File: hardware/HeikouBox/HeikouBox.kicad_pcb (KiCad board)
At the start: 2 copper layers, 0 parts

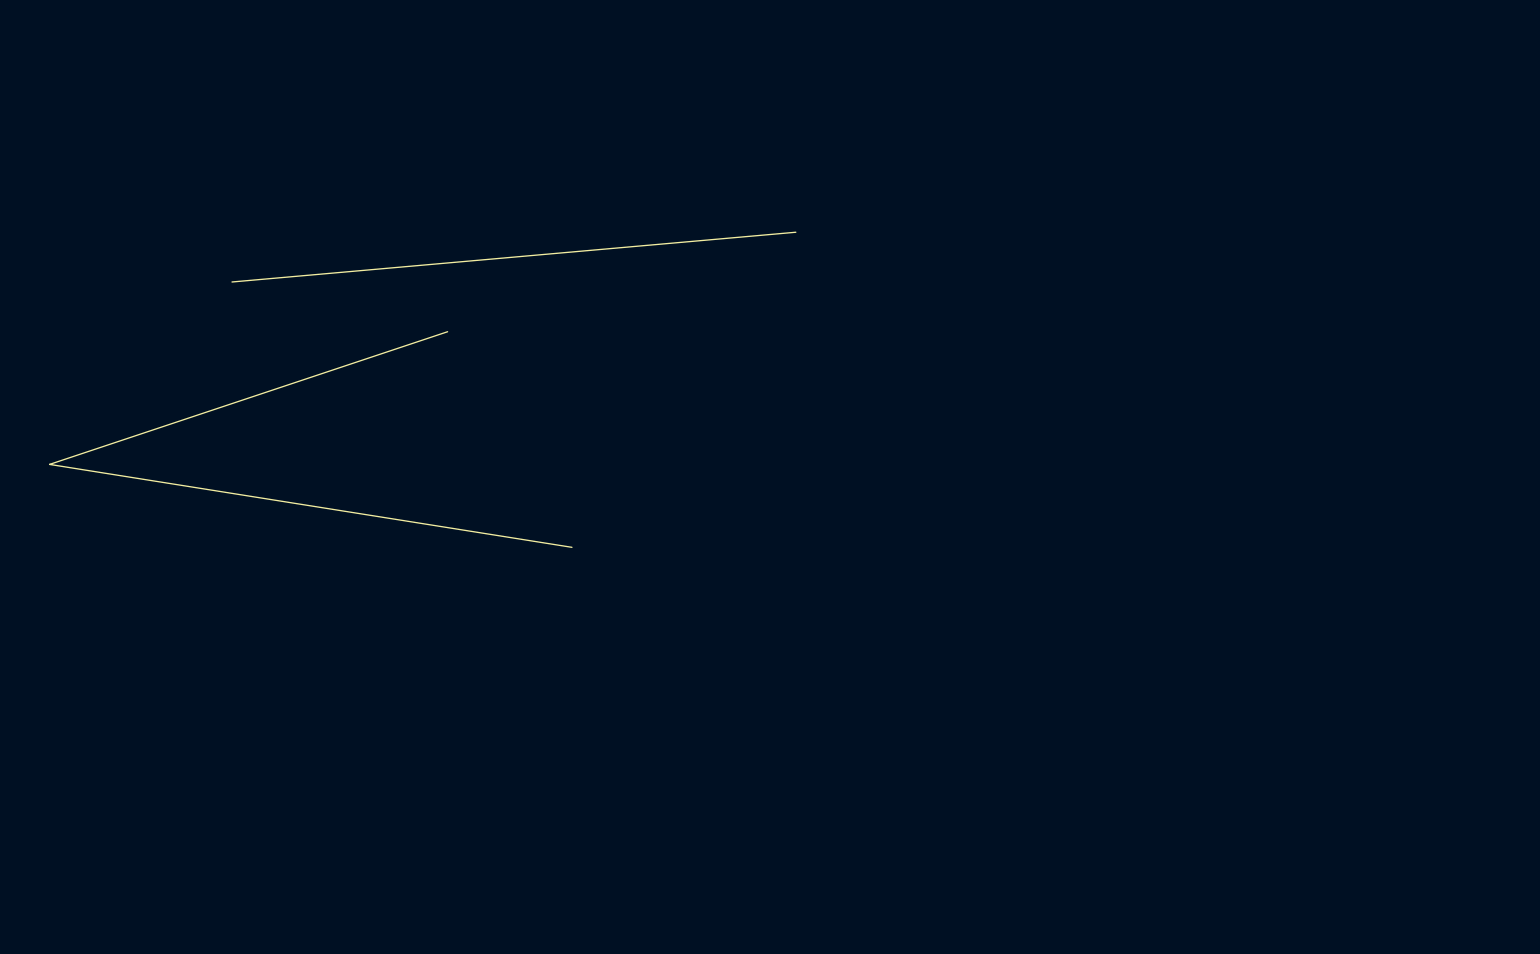
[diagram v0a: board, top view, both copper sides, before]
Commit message: Tidy up and split to multi sheet
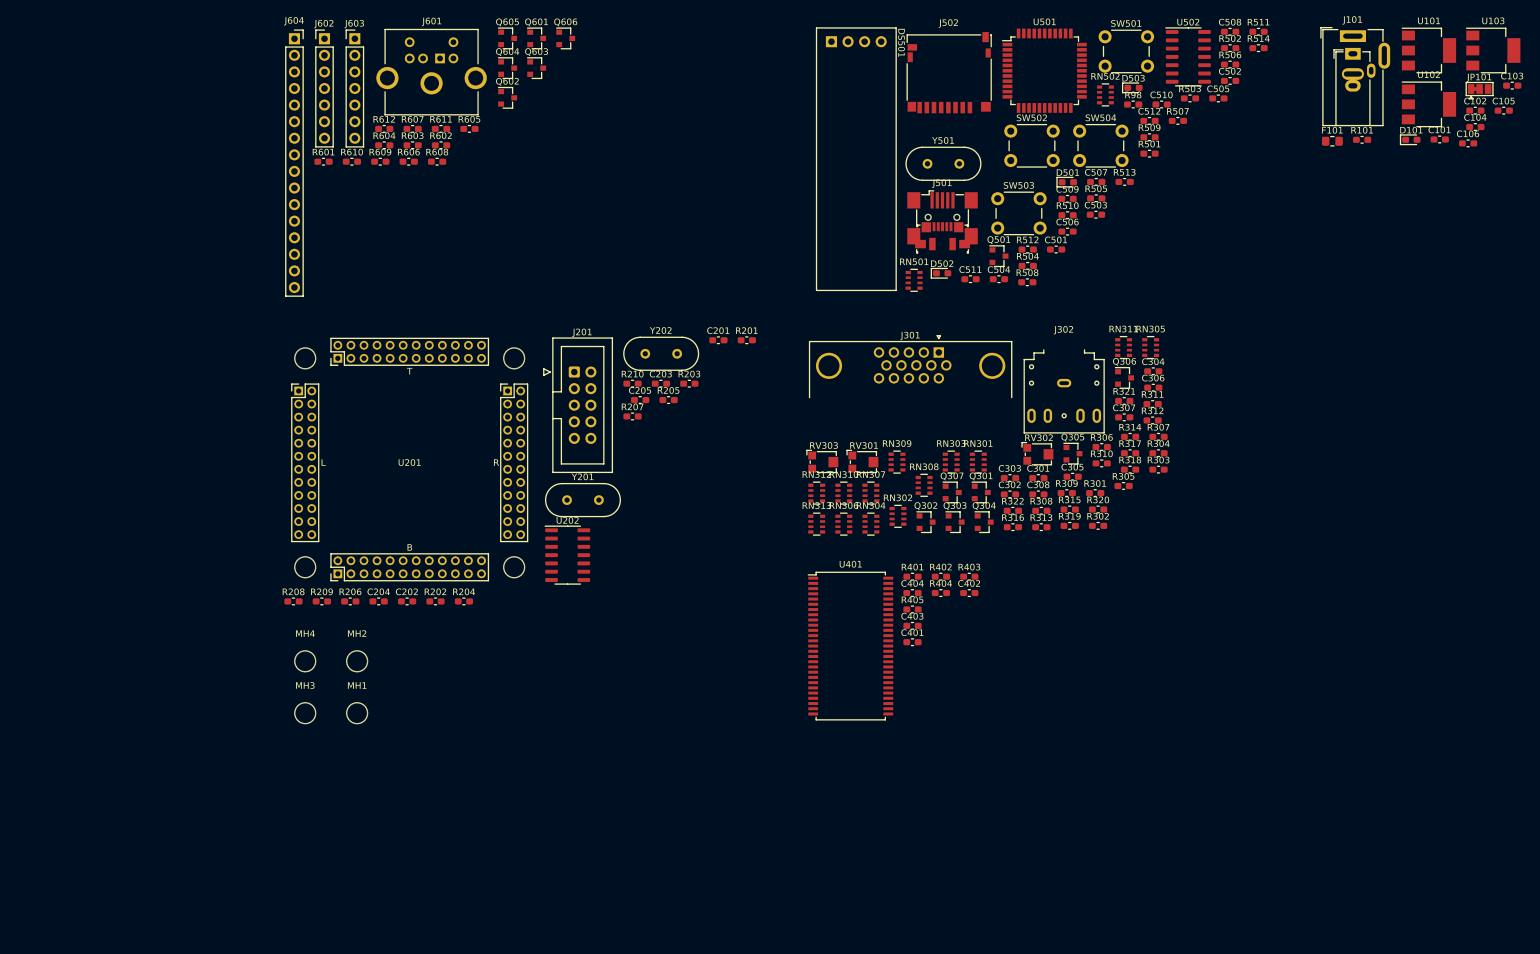
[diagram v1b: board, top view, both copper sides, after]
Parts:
- added C101: 10u, Capacitor_SMD:C_0603_1608Metric_Pad1.05x0.95mm_HandSolder, F.Cu at (233.2, 34.1)
- added C102: 100n, Capacitor_SMD:C_0603_1608Metric_Pad1.05x0.95mm_HandSolder, F.Cu at (238.7, 29.6)
- added C103: 100n, Capacitor_SMD:C_0603_1608Metric_Pad1.05x0.95mm_HandSolder, F.Cu at (244.3, 25.8)
- added C104: 10u, Capacitor_SMD:C_0603_1608Metric_Pad1.05x0.95mm_HandSolder, F.Cu at (238.7, 32.1)
- added C105: 10u, Capacitor_SMD:C_0603_1608Metric_Pad1.05x0.95mm_HandSolder, F.Cu at (243.0, 29.6)
- added C106: 10u, Capacitor_SMD:C_0603_1608Metric_Pad1.05x0.95mm_HandSolder, F.Cu at (237.6, 34.7)
- added C201: 100n, Capacitor_SMD:C_0603_1608Metric_Pad1.05x0.95mm_HandSolder, F.Cu at (122.8, 64.8)
- added C202: 22p, Capacitor_SMD:C_0603_1608Metric_Pad1.05x0.95mm_HandSolder, F.Cu at (75.1, 104.8)
- added C203: 22p, Capacitor_SMD:C_0603_1608Metric_Pad1.05x0.95mm_HandSolder, F.Cu at (114.0, 71.5)
- added C204: 22p, Capacitor_SMD:C_0603_1608Metric_Pad1.05x0.95mm_HandSolder, F.Cu at (70.7, 104.8)
- added C205: 22p, Capacitor_SMD:C_0603_1608Metric_Pad1.05x0.95mm_HandSolder, F.Cu at (110.8, 74.0)
- added C301: 10u, Capacitor_SMD:C_0603_1608Metric_Pad1.05x0.95mm_HandSolder, F.Cu at (171.8, 85.9)
- added C302: 10u, Capacitor_SMD:C_0603_1608Metric_Pad1.05x0.95mm_HandSolder, F.Cu at (167.4, 88.4)
- added C303: 10n, Capacitor_SMD:C_0603_1608Metric_Pad1.05x0.95mm_HandSolder, F.Cu at (167.4, 85.9)
- added C304: 10n, Capacitor_SMD:C_0603_1608Metric_Pad1.05x0.95mm_HandSolder, F.Cu at (189.4, 69.6)
- added C305: 1u, Capacitor_SMD:C_0603_1608Metric_Pad1.05x0.95mm_HandSolder, F.Cu at (177.0, 85.7)
- added C306: 1u, Capacitor_SMD:C_0603_1608Metric_Pad1.05x0.95mm_HandSolder, F.Cu at (189.4, 72.1)
- added C307: 1u, Capacitor_SMD:C_0603_1608Metric_Pad1.05x0.95mm_HandSolder, F.Cu at (184.9, 76.6)
- added C308: 1u, Capacitor_SMD:C_0603_1608Metric_Pad1.05x0.95mm_HandSolder, F.Cu at (171.8, 88.4)
- added C401: 100n, Capacitor_SMD:C_0603_1608Metric_Pad1.05x0.95mm_HandSolder, F.Cu at (152.5, 111.1)
- added C402: 100n, Capacitor_SMD:C_0603_1608Metric_Pad1.05x0.95mm_HandSolder, F.Cu at (161.2, 103.5)
- added C403: 100n, Capacitor_SMD:C_0603_1608Metric_Pad1.05x0.95mm_HandSolder, F.Cu at (152.5, 108.5)
- added C404: 100n, Capacitor_SMD:C_0603_1608Metric_Pad1.05x0.95mm_HandSolder, F.Cu at (152.5, 103.5)
- added C501: 100n, Capacitor_SMD:C_0603_1608Metric_Pad1.05x0.95mm_HandSolder, F.Cu at (174.5, 50.9)
- added C502: 100n, Capacitor_SMD:C_0603_1608Metric_Pad1.05x0.95mm_HandSolder, F.Cu at (201.1, 25.1)
- added C503: 100n, Capacitor_SMD:C_0603_1608Metric_Pad1.05x0.95mm_HandSolder, F.Cu at (180.6, 45.6)
- added C504: 100n, Capacitor_SMD:C_0603_1608Metric_Pad1.05x0.95mm_HandSolder, F.Cu at (165.7, 55.5)
- added C505: 100n, Capacitor_SMD:C_0603_1608Metric_Pad1.05x0.95mm_HandSolder, F.Cu at (199.3, 27.8)
- added C506: 100n, Capacitor_SMD:C_0603_1608Metric_Pad1.05x0.95mm_HandSolder, F.Cu at (176.2, 48.2)
- added C507: 22p, Capacitor_SMD:C_0603_1608Metric_Pad1.05x0.95mm_HandSolder, F.Cu at (180.6, 40.6)
- added C508: 22p, Capacitor_SMD:C_0603_1608Metric_Pad1.05x0.95mm_HandSolder, F.Cu at (201.1, 17.6)
- added C509: 100n, Capacitor_SMD:C_0603_1608Metric_Pad1.05x0.95mm_HandSolder, F.Cu at (176.2, 43.1)
- added C510: 100n, Capacitor_SMD:C_0603_1608Metric_Pad1.05x0.95mm_HandSolder, F.Cu at (190.6, 28.7)
- added C511: 100n, Capacitor_SMD:C_0603_1608Metric_Pad1.05x0.95mm_HandSolder, F.Cu at (161.4, 55.5)
- added C512: 100n, Capacitor_SMD:C_0603_1608Metric_Pad1.05x0.95mm_HandSolder, F.Cu at (188.8, 31.2)
- added D101: Power, LED_SMD:LED_0603_1608Metric_Pad1.05x0.95mm_HandSolder, F.Cu at (228.9, 34.1)
- added D501: RX, LED_SMD:LED_0603_1608Metric_Pad1.05x0.95mm_HandSolder, F.Cu at (176.3, 40.6)
- added D502: TX, LED_SMD:LED_0603_1608Metric_Pad1.05x0.95mm_HandSolder, F.Cu at (157.0, 54.5)
- added D503: LOAD, LED_SMD:LED_0603_1608Metric_Pad1.05x0.95mm_HandSolder, F.Cu at (186.3, 26.1)
- added DS501: OLED-4P-I2C, KSK_HeikouBox:OLED-4P-Generic-128x32-0.91in, F.Cu at (140.1, 19.1)
- added F101: Poly 0.5A, Fuse:Fuse_0805_2012Metric_Pad1.15x1.40mm_HandSolder, F.Cu at (216.8, 34.3)
- added J101: Barrel_Jack_Switch, KSK_HeikouBox:BarrelJack_Multi, F.Cu at (219.9, 18.2)
- added J201: Conn_02x05_Odd_Even, Connector_IDC:IDC-Header_2x05_P2.54mm_Vertical, F.Cu at (100.7, 69.7)
- added J301: DB15_Female_HighDensity_MountingHoles, Connector_Dsub:DSUB-15-HD_Female_Horizontal_P2.29x1.98mm_EdgePinOffset3.03mm_Housed_MountingHolesOffset4.94mm, F.Cu at (156.5, 66.7)
- added J302: AudioJack3_SwitchTR, KSK_HeikouBox:Jack_3.5mm_PJ307_Horizontal_NoHoles, F.Cu at (175.7, 71.4)
- added J501: USB_B_Micro, KSK_HeikouBox:USB_Mini-Micro-B_Multi, F.Cu at (157.1, 46.0)
- added J502: Micro_SD_Card_Det, Connector_Card:microSD_HC_Hirose_DM3D-SF, F.Cu at (158.1, 23.8)
- added J601: PS/2 Keyboard, KSK_HeikouBox:TE_Mini-DIN-6_Horizontal, F.Cu at (80.1, 21.6)
- added J602: Conn_01x07, Connector_PinHeader_2.54mm:PinHeader_1x07_P2.54mm_Vertical, F.Cu at (62.4, 18.6)
- added J603: Conn_01x07, Connector_PinHeader_2.54mm:PinHeader_1x07_P2.54mm_Vertical, F.Cu at (67.1, 18.6)
- added J604: Conn_01x16, Connector_PinSocket_2.54mm:PinSocket_1x16_P2.54mm_Vertical, F.Cu at (57.8, 18.6)
- added JP101: SolderJumper_3_Bridged12, Jumper:SolderJumper-3_P1.3mm_Bridged12_Pad1.0x1.5mm, F.Cu at (239.3, 26.3)
- added MH1: MountingHole, MountingHole:MountingHole_3.2mm_M3, F.Cu at (67.4, 121.9)
- added MH2: MountingHole, MountingHole:MountingHole_3.2mm_M3, F.Cu at (67.4, 114.0)
- added MH3: MountingHole, MountingHole:MountingHole_3.2mm_M3, F.Cu at (59.5, 121.9)
- added MH4: MountingHole, MountingHole:MountingHole_3.2mm_M3, F.Cu at (59.5, 114.0)
- added Q301: MMBT3904, Package_TO_SOT_SMD:SOT-23, F.Cu at (163.0, 88.1)
- added Q302: MMBT3904, Package_TO_SOT_SMD:SOT-23, F.Cu at (154.6, 92.7)
- added Q303: MMBT3904, Package_TO_SOT_SMD:SOT-23, F.Cu at (159.0, 92.7)
- added Q304: MMBT3904, Package_TO_SOT_SMD:SOT-23, F.Cu at (163.5, 92.7)
- added Q305: MMBT3904, Package_TO_SOT_SMD:SOT-23, F.Cu at (177.1, 82.2)
- added Q306: MMBT3904, Package_TO_SOT_SMD:SOT-23, F.Cu at (185.0, 70.6)
- added Q307: MMBT3904, Package_TO_SOT_SMD:SOT-23, F.Cu at (158.6, 88.1)
- added Q501: MMBT3906, Package_TO_SOT_SMD:SOT-23, F.Cu at (165.7, 51.9)
- added Q601: BSS138, Package_TO_SOT_SMD:SOT-23, F.Cu at (94.9, 18.6)
- added Q602: BSS138, Package_TO_SOT_SMD:SOT-23, F.Cu at (90.5, 27.7)
- added Q603: BSS138, Package_TO_SOT_SMD:SOT-23, F.Cu at (94.9, 23.1)
- added Q604: BSS138, Package_TO_SOT_SMD:SOT-23, F.Cu at (90.5, 23.1)
- added Q605: BSS138, Package_TO_SOT_SMD:SOT-23, F.Cu at (90.5, 18.6)
- added Q606: BSS138, Package_TO_SOT_SMD:SOT-23, F.Cu at (99.4, 18.6)
- added R101: 1K, Resistor_SMD:R_0603_1608Metric_Pad1.05x0.95mm_HandSolder, F.Cu at (221.3, 34.1)
- added R201: 1M, Resistor_SMD:R_0603_1608Metric_Pad1.05x0.95mm_HandSolder, F.Cu at (127.1, 64.8)
- added R202: 1M, Resistor_SMD:R_0603_1608Metric_Pad1.05x0.95mm_HandSolder, F.Cu at (79.4, 104.8)
- added R203: 1K, Resistor_SMD:R_0603_1608Metric_Pad1.05x0.95mm_HandSolder, F.Cu at (118.3, 71.5)
- added R204: 1K, Resistor_SMD:R_0603_1608Metric_Pad1.05x0.95mm_HandSolder, F.Cu at (83.8, 104.8)
- added R205: 10K, Resistor_SMD:R_0603_1608Metric_Pad1.05x0.95mm_HandSolder, F.Cu at (115.1, 74.0)
- added R206: 10K, Resistor_SMD:R_0603_1608Metric_Pad1.05x0.95mm_HandSolder, F.Cu at (66.4, 104.8)
- added R207: 10K, Resistor_SMD:R_0603_1608Metric_Pad1.05x0.95mm_HandSolder, F.Cu at (109.6, 76.5)
- added R208: 10K, Resistor_SMD:R_0603_1608Metric_Pad1.05x0.95mm_HandSolder, F.Cu at (57.7, 104.8)
- added R209: 10K, Resistor_SMD:R_0603_1608Metric_Pad1.05x0.95mm_HandSolder, F.Cu at (62.0, 104.8)
- added R210: 10K, Resistor_SMD:R_0603_1608Metric_Pad1.05x0.95mm_HandSolder, F.Cu at (109.6, 71.5)
- added R301: 75R, Resistor_SMD:R_0603_1608Metric_Pad1.05x0.95mm_HandSolder, F.Cu at (180.5, 88.2)
- added R302: 75R, Resistor_SMD:R_0603_1608Metric_Pad1.05x0.95mm_HandSolder, F.Cu at (180.9, 93.2)
- added R303: 75R, Resistor_SMD:R_0603_1608Metric_Pad1.05x0.95mm_HandSolder, F.Cu at (190.2, 84.6)
- added R304: 1K, Resistor_SMD:R_0603_1608Metric_Pad1.05x0.95mm_HandSolder, F.Cu at (190.2, 82.1)
- added R305: 1K, Resistor_SMD:R_0603_1608Metric_Pad1.05x0.95mm_HandSolder, F.Cu at (184.8, 87.1)
- added R306: 1K, Resistor_SMD:R_0603_1608Metric_Pad1.05x0.95mm_HandSolder, F.Cu at (181.5, 81.2)
- added R307: 1K, Resistor_SMD:R_0603_1608Metric_Pad1.05x0.95mm_HandSolder, F.Cu at (190.2, 79.6)
- added R308: 1K, Resistor_SMD:R_0603_1608Metric_Pad1.05x0.95mm_HandSolder, F.Cu at (172.2, 90.9)
- added R309: 1K, Resistor_SMD:R_0603_1608Metric_Pad1.05x0.95mm_HandSolder, F.Cu at (176.1, 88.2)
- added R310: 1K, Resistor_SMD:R_0603_1608Metric_Pad1.05x0.95mm_HandSolder, F.Cu at (181.5, 83.7)
- added R311: 2K2, Resistor_SMD:R_0603_1608Metric_Pad1.05x0.95mm_HandSolder, F.Cu at (189.3, 74.6)
- added R312: 2K2, Resistor_SMD:R_0603_1608Metric_Pad1.05x0.95mm_HandSolder, F.Cu at (189.3, 77.1)
- added R313: 1K, Resistor_SMD:R_0603_1608Metric_Pad1.05x0.95mm_HandSolder, F.Cu at (172.2, 93.4)
- added R314: 1K, Resistor_SMD:R_0603_1608Metric_Pad1.05x0.95mm_HandSolder, F.Cu at (185.8, 79.6)
- added R315: 1K, Resistor_SMD:R_0603_1608Metric_Pad1.05x0.95mm_HandSolder, F.Cu at (176.6, 90.7)
- added R316: 1K, Resistor_SMD:R_0603_1608Metric_Pad1.05x0.95mm_HandSolder, F.Cu at (167.9, 93.4)
- added R317: 10K, Resistor_SMD:R_0603_1608Metric_Pad1.05x0.95mm_HandSolder, F.Cu at (185.8, 82.1)
- added R318: 10K, Resistor_SMD:R_0603_1608Metric_Pad1.05x0.95mm_HandSolder, F.Cu at (185.8, 84.6)
- added R319: 10K, Resistor_SMD:R_0603_1608Metric_Pad1.05x0.95mm_HandSolder, F.Cu at (176.6, 93.2)
- added R320: 10K, Resistor_SMD:R_0603_1608Metric_Pad1.05x0.95mm_HandSolder, F.Cu at (180.9, 90.7)
- added R321: 10K, Resistor_SMD:R_0603_1608Metric_Pad1.05x0.95mm_HandSolder, F.Cu at (184.9, 74.1)
- added R322: 10K, Resistor_SMD:R_0603_1608Metric_Pad1.05x0.95mm_HandSolder, F.Cu at (167.9, 90.9)
- added R401: 1K, Resistor_SMD:R_0603_1608Metric_Pad1.05x0.95mm_HandSolder, F.Cu at (152.5, 101.0)
- added R402: 1K, Resistor_SMD:R_0603_1608Metric_Pad1.05x0.95mm_HandSolder, F.Cu at (156.8, 101.0)
- added R403: 1K, Resistor_SMD:R_0603_1608Metric_Pad1.05x0.95mm_HandSolder, F.Cu at (161.2, 101.0)
- added R404: 1K, Resistor_SMD:R_0603_1608Metric_Pad1.05x0.95mm_HandSolder, F.Cu at (156.8, 103.5)
- added R405: 1K, Resistor_SMD:R_0603_1608Metric_Pad1.05x0.95mm_HandSolder, F.Cu at (152.5, 106.0)
- added R501: 1K, Resistor_SMD:R_0603_1608Metric_Pad1.05x0.95mm_HandSolder, F.Cu at (188.8, 36.2)
- added R502: 1K, Resistor_SMD:R_0603_1608Metric_Pad1.05x0.95mm_HandSolder, F.Cu at (201.1, 20.1)
- added R503: 1K, Resistor_SMD:R_0603_1608Metric_Pad1.05x0.95mm_HandSolder, F.Cu at (195.0, 27.8)
- added R504: 1K, Resistor_SMD:R_0603_1608Metric_Pad1.05x0.95mm_HandSolder, F.Cu at (170.1, 53.4)
- added R505: 1K, Resistor_SMD:R_0603_1608Metric_Pad1.05x0.95mm_HandSolder, F.Cu at (180.6, 43.1)
- added R506: 1K, Resistor_SMD:R_0603_1608Metric_Pad1.05x0.95mm_HandSolder, F.Cu at (201.1, 22.6)
- added R507: 1K, Resistor_SMD:R_0603_1608Metric_Pad1.05x0.95mm_HandSolder, F.Cu at (193.1, 31.2)
- added R508: 1K, Resistor_SMD:R_0603_1608Metric_Pad1.05x0.95mm_HandSolder, F.Cu at (170.1, 55.9)
- added R509: 1K, Resistor_SMD:R_0603_1608Metric_Pad1.05x0.95mm_HandSolder, F.Cu at (188.8, 33.7)
- added R510: 1K, Resistor_SMD:R_0603_1608Metric_Pad1.05x0.95mm_HandSolder, F.Cu at (176.2, 45.7)
- added R511: 10K, Resistor_SMD:R_0603_1608Metric_Pad1.05x0.95mm_HandSolder, F.Cu at (205.5, 17.6)
- added R512: 10K, Resistor_SMD:R_0603_1608Metric_Pad1.05x0.95mm_HandSolder, F.Cu at (170.1, 50.9)
- added R513: 10K, Resistor_SMD:R_0603_1608Metric_Pad1.05x0.95mm_HandSolder, F.Cu at (185.0, 40.6)
- added R514: 10K, Resistor_SMD:R_0603_1608Metric_Pad1.05x0.95mm_HandSolder, F.Cu at (205.5, 20.1)
- added R601: 10K, Resistor_SMD:R_0603_1608Metric_Pad1.05x0.95mm_HandSolder, F.Cu at (62.3, 37.5)
- added R602: 10K, Resistor_SMD:R_0603_1608Metric_Pad1.05x0.95mm_HandSolder, F.Cu at (80.3, 34.9)
- added R603: 10K, Resistor_SMD:R_0603_1608Metric_Pad1.05x0.95mm_HandSolder, F.Cu at (75.9, 34.9)
- added R604: 10K, Resistor_SMD:R_0603_1608Metric_Pad1.05x0.95mm_HandSolder, F.Cu at (71.6, 34.9)
- added R605: 10K, Resistor_SMD:R_0603_1608Metric_Pad1.05x0.95mm_HandSolder, F.Cu at (84.6, 32.4)
- added R606: 10K, Resistor_SMD:R_0603_1608Metric_Pad1.05x0.95mm_HandSolder, F.Cu at (75.3, 37.5)
- added R607: 2K2, Resistor_SMD:R_0603_1608Metric_Pad1.05x0.95mm_HandSolder, F.Cu at (75.9, 32.4)
- added R608: 2K2, Resistor_SMD:R_0603_1608Metric_Pad1.05x0.95mm_HandSolder, F.Cu at (79.7, 37.5)
- added R609: 2K2, Resistor_SMD:R_0603_1608Metric_Pad1.05x0.95mm_HandSolder, F.Cu at (71.0, 37.5)
- added R610: 2K2, Resistor_SMD:R_0603_1608Metric_Pad1.05x0.95mm_HandSolder, F.Cu at (66.6, 37.5)
- added R611: 2K2, Resistor_SMD:R_0603_1608Metric_Pad1.05x0.95mm_HandSolder, F.Cu at (80.3, 32.4)
- added R612: 2K2, Resistor_SMD:R_0603_1608Metric_Pad1.05x0.95mm_HandSolder, F.Cu at (71.6, 32.4)
- added R98: 2K2, Resistor_SMD:R_0603_1608Metric_Pad1.05x0.95mm_HandSolder, F.Cu at (186.3, 28.7)
- added RN301: 2K2, Resistor_SMD:R_Array_Convex_4x0603, F.Cu at (162.6, 83.5)
- added RN302: 2K2, Resistor_SMD:R_Array_Convex_4x0603, F.Cu at (150.3, 91.8)
- added RN303: 2K2, Resistor_SMD:R_Array_Convex_4x0603, F.Cu at (158.4, 83.5)
- added RN304: 2K2, Resistor_SMD:R_Array_Convex_4x0603, F.Cu at (146.1, 93.0)
- added RN305: 2K2, Resistor_SMD:R_Array_Convex_4x0603, F.Cu at (189.0, 65.9)
- added RN306: 2K2, Resistor_SMD:R_Array_Convex_4x0603, F.Cu at (142.0, 93.0)
- added RN307: 2K2, Resistor_SMD:R_Array_Convex_4x0603, F.Cu at (146.1, 88.2)
- added RN308: 2K2, Resistor_SMD:R_Array_Convex_4x0603, F.Cu at (154.3, 87.0)
- added RN309: 2K2, Resistor_SMD:R_Array_Convex_4x0603, F.Cu at (150.1, 83.5)
- added RN310: 2K2, Resistor_SMD:R_Array_Convex_4x0603, F.Cu at (142.0, 88.2)
- added RN311: 2K2, Resistor_SMD:R_Array_Convex_4x0603, F.Cu at (184.8, 65.9)
- added RN312: 2K2, Resistor_SMD:R_Array_Convex_4x0603, F.Cu at (137.8, 88.2)
- added RN313: 2K2, Resistor_SMD:R_Array_Convex_4x0603, F.Cu at (137.8, 93.0)
- added RN501: 2K2, Resistor_SMD:R_Array_Convex_4x0603, F.Cu at (152.7, 55.6)
- added RN502: 2K2, Resistor_SMD:R_Array_Convex_4x0603, F.Cu at (182.0, 27.2)
- added RV301: 1K, Potentiometer_SMD:Potentiometer_Bourns_TC33X_Vertical, F.Cu at (145.1, 83.5)
- added RV302: 1K, Potentiometer_SMD:Potentiometer_Bourns_TC33X_Vertical, F.Cu at (171.9, 82.3)
- added RV303: 1K, Potentiometer_SMD:Potentiometer_Bourns_TC33X_Vertical, F.Cu at (138.9, 83.5)
- added SW501: SW_Push, Button_Switch_THT:SW_PUSH_6mm_H5mm, F.Cu at (182.0, 18.3)
- added SW502: SW_Push, Button_Switch_THT:SW_PUSH_6mm_H5mm, F.Cu at (167.5, 32.8)
- added SW503: SW_Push, Button_Switch_THT:SW_PUSH_6mm_H5mm, F.Cu at (165.5, 43.1)
- added SW504: SW_Push, Button_Switch_THT:SW_PUSH_6mm_H5mm, F.Cu at (178.1, 32.8)
- added U101: LD1117S33TR, Package_TO_SOT_SMD:SOT-223-3_TabPin2, F.Cu at (231.6, 20.4)
- added U102: LD1117S25TR, Package_TO_SOT_SMD:SOT-223-3_TabPin2, F.Cu at (231.6, 28.7)
- added U103: LD1117S12TR, Package_TO_SOT_SMD:SOT-223-3_TabPin2, F.Cu at (241.4, 20.4)
- added U201: HeikouBox-Core, KSK_HeikouBox:HeikouBox-Core-Base, F.Cu at (75.5, 83.6)
- added U202: 74HCU04, Package_SO:SOIC-14_3.9x8.7mm_P1.27mm, F.Cu at (99.7, 97.7)
- added U401: K4S281632-UC60, Package_SO:TSOP-II-54_22.2x10.16mm_P0.8mm, F.Cu at (143.0, 111.6)
- added U501: ATmega644PA-AU, Package_QFP:TQFP-44_10x10mm_P0.8mm, F.Cu at (172.7, 23.5)
- added U502: MCP2221AxSL, Package_SO:SOIC-14_3.9x8.7mm_P1.27mm, F.Cu at (194.7, 21.4)
- added Y201: 14.31818MHz, Crystal:Crystal_HC49-4H_Vertical, F.Cu at (99.6, 89.3)
- added Y202: 28.37516MHz, Crystal:Crystal_HC49-4H_Vertical, F.Cu at (111.6, 66.9)
- added Y501: 8MHz, Crystal:Crystal_HC49-4H_Vertical, F.Cu at (154.8, 37.8)
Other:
- net class Default: clearance 0.2 -> 0.175; trace_width 0.25 -> 0.175; via_dia 0.8 -> 0.6; via_drill 0.4 -> 0.3
- net class Power added: clearance 0.195, trace_width 1.016, via_dia 0.6, via_drill 0.3
- net class Signal added: clearance 0.175, trace_width 0.175, via_dia 0.6, via_drill 0.3
- rule pad_to_mask_clearance: 0.2 -> 0.05
- rule trace_clearance: 0.2 -> 0.175
- rule trace_min: 0.2 -> 0.127
- rule via_min_size: 0.4 -> 0.6

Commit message: Mostly routed board
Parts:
- removed C103, C505, C506, C509, C510, C511, C512: 100n, Capacitor_SMD:C_0603_1608Metric_Pad1.05x0.95mm_HandSolder
- removed C507, C508: 22p, Capacitor_SMD:C_0603_1608Metric_Pad1.05x0.95mm_HandSolder
- removed J601: PS/2 Keyboard, KSK_HeikouBox:TE_Mini-DIN-6_Horizontal
- removed J602, J603: Conn_01x07, Connector_PinHeader_2.54mm:PinHeader_1x07_P2.54mm_Vertical
- removed J604: Conn_01x16, Connector_PinSocket_2.54mm:PinSocket_1x16_P2.54mm_Vertical
- removed Q601, Q602, Q603, Q604, Q605, Q606: BSS138, Package_TO_SOT_SMD:SOT-23
- removed R601, R602, R603, R604, R605, R606: 10K, Resistor_SMD:R_0603_1608Metric_Pad1.05x0.95mm_HandSolder
- removed R607, R608, R609, R610, R611, R612, R98: 2K2, Resistor_SMD:R_0603_1608Metric_Pad1.05x0.95mm_HandSolder
- removed RN301, RN302, RN303, RN304, RN305, RN306, RN307, RN308, RN309, RN310, RN311, RN312, RN313, RN501, RN502: 2K2, Resistor_SMD:R_Array_Convex_4x0603
- removed U502: MCP2221AxSL, Package_SO:SOIC-14_3.9x8.7mm_P1.27mm
- removed Y501: 8MHz, Crystal:Crystal_HC49-4H_Vertical
- added C405: 100n, Capacitor_SMD:C_0603_1608Metric_Pad1.08x0.95mm_HandSolder, F.Cu at (105.2, 140.0)
- added D504: WS2812B, LED_SMD:LED_WS2812B_PLCC4_5.0x5.0mm_P3.2mm, B.Cu at (190.2, 66.8)
- added J202: Conn_02x08_Odd_Even, Connector_PinHeader_2.54mm:PinHeader_2x08_P2.54mm_Vertical, F.Cu at (95.2, 117.2)
- added J503: PS/2, KSK_HeikouBox:TE_Mini-DIN-6_Horizontal, F.Cu at (187.4, 105.6)
- added JP501: RGB Bypass, Jumper:SolderJumper-2_P1.3mm_Open_RoundedPad1.0x1.5mm, F.Cu at (182.0, 68.4)
- added JP502: DVCC, Jumper:SolderJumper-3_P1.3mm_Open_RoundedPad1.0x1.5mm, B.Cu at (150.6, 118.0)
- added JP503: DGND, Jumper:SolderJumper-3_P1.3mm_Open_RoundedPad1.0x1.5mm, B.Cu at (147.8, 118.0)
- added Q502: BSS138, Package_TO_SOT_SMD:SOT-23, F.Cu at (187.0, 94.6)
- added Q503: BSS138, Package_TO_SOT_SMD:SOT-23, F.Cu at (183.4, 94.6)
- added R323: 2K2, Resistor_SMD:R_0603_1608Metric_Pad0.98x0.95mm_HandSolder, F.Cu at (96.6, 95.8)
- added R324: 2K2, Resistor_SMD:R_0603_1608Metric_Pad0.98x0.95mm_HandSolder, F.Cu at (93.2, 95.8)
- added R325: 2K2, Resistor_SMD:R_0603_1608Metric_Pad0.98x0.95mm_HandSolder, F.Cu at (92.4, 93.2)
- added R326: 2K2, Resistor_SMD:R_0603_1608Metric_Pad0.98x0.95mm_HandSolder, F.Cu at (94.0, 93.2)
- added R327: 2K2, Resistor_SMD:R_0603_1608Metric_Pad0.98x0.95mm_HandSolder, F.Cu at (96.6, 92.4)
- added R328: 2K2, Resistor_SMD:R_0603_1608Metric_Pad0.98x0.95mm_HandSolder, F.Cu at (92.4, 89.8)
- added R329: 2K2, Resistor_SMD:R_0603_1608Metric_Pad0.98x0.95mm_HandSolder, F.Cu at (94.0, 89.8)
- added R330: 2K2, Resistor_SMD:R_0603_1608Metric_Pad0.98x0.95mm_HandSolder, F.Cu at (96.6, 89.0)
- added R331: 2K2, Resistor_SMD:R_0603_1608Metric_Pad0.98x0.95mm_HandSolder, F.Cu at (92.4, 86.4)
- added R332: 2K2, Resistor_SMD:R_0603_1608Metric_Pad0.98x0.95mm_HandSolder, F.Cu at (94.0, 86.4)
- added R333: 2K2, Resistor_SMD:R_0603_1608Metric_Pad0.98x0.95mm_HandSolder, F.Cu at (96.6, 85.6)
- added R334: 2K2, Resistor_SMD:R_0603_1608Metric_Pad0.98x0.95mm_HandSolder, F.Cu at (92.4, 83.0)
- added R335: 2K2, Resistor_SMD:R_0603_1608Metric_Pad0.98x0.95mm_HandSolder, F.Cu at (94.0, 83.0)
- added R336: 2K2, Resistor_SMD:R_0603_1608Metric_Pad0.98x0.95mm_HandSolder, F.Cu at (96.6, 82.2)
- added R337: 2K2, Resistor_SMD:R_0603_1608Metric_Pad0.98x0.95mm_HandSolder, F.Cu at (104.0, 76.8)
- added R338: 2K2, Resistor_SMD:R_0603_1608Metric_Pad0.98x0.95mm_HandSolder, F.Cu at (107.4, 99.2)
- added R339: 2K2, Resistor_SMD:R_0603_1608Metric_Pad0.98x0.95mm_HandSolder, F.Cu at (104.0, 99.2)
- added R340: 2K2, Resistor_SMD:R_0603_1608Metric_Pad0.98x0.95mm_HandSolder, F.Cu at (103.2, 96.6)
- added R341: 2K2, Resistor_SMD:R_0603_1608Metric_Pad0.98x0.95mm_HandSolder, F.Cu at (104.8, 96.6)
- added R342: 2K2, Resistor_SMD:R_0603_1608Metric_Pad0.98x0.95mm_HandSolder, F.Cu at (107.4, 95.8)
- added R343: 2K2, Resistor_SMD:R_0603_1608Metric_Pad0.98x0.95mm_HandSolder, F.Cu at (103.2, 93.2)
- added R344: 2K2, Resistor_SMD:R_0603_1608Metric_Pad0.98x0.95mm_HandSolder, F.Cu at (104.8, 93.2)
- added R345: 2K2, Resistor_SMD:R_0603_1608Metric_Pad0.98x0.95mm_HandSolder, F.Cu at (107.4, 92.4)
- added R346: 2K2, Resistor_SMD:R_0603_1608Metric_Pad0.98x0.95mm_HandSolder, F.Cu at (103.2, 89.8)
- added R347: 2K2, Resistor_SMD:R_0603_1608Metric_Pad0.98x0.95mm_HandSolder, F.Cu at (104.8, 89.8)
- added R348: 2K2, Resistor_SMD:R_0603_1608Metric_Pad0.98x0.95mm_HandSolder, F.Cu at (107.4, 89.0)
- added R349: 2K2, Resistor_SMD:R_0603_1608Metric_Pad0.98x0.95mm_HandSolder, F.Cu at (103.2, 86.4)
- added R350: 2K2, Resistor_SMD:R_0603_1608Metric_Pad0.98x0.95mm_HandSolder, F.Cu at (104.8, 86.4)
- added R351: 2K2, Resistor_SMD:R_0603_1608Metric_Pad0.98x0.95mm_HandSolder, F.Cu at (107.4, 85.6)
- added R352: 2K2, Resistor_SMD:R_0603_1608Metric_Pad0.98x0.95mm_HandSolder, F.Cu at (103.2, 83.0)
- added R353: 2K2, Resistor_SMD:R_0603_1608Metric_Pad0.98x0.95mm_HandSolder, F.Cu at (104.8, 83.0)
- added R354: 2K2, Resistor_SMD:R_0603_1608Metric_Pad0.98x0.95mm_HandSolder, F.Cu at (107.4, 82.2)
- added R355: 2K2, Resistor_SMD:R_0603_1608Metric_Pad0.98x0.95mm_HandSolder, F.Cu at (107.6, 76.8)
- added R356: 2K2, Resistor_SMD:R_0603_1608Metric_Pad0.98x0.95mm_HandSolder, F.Cu at (118.2, 96.2)
- added R357: 2K2, Resistor_SMD:R_0603_1608Metric_Pad0.98x0.95mm_HandSolder, F.Cu at (114.8, 96.2)
- added R358: 2K2, Resistor_SMD:R_0603_1608Metric_Pad0.98x0.95mm_HandSolder, F.Cu at (114.0, 93.6)
- added R359: 2K2, Resistor_SMD:R_0603_1608Metric_Pad0.98x0.95mm_HandSolder, F.Cu at (115.6, 93.6)
- added R360: 2K2, Resistor_SMD:R_0603_1608Metric_Pad0.98x0.95mm_HandSolder, F.Cu at (118.2, 92.8)
- added R361: 2K2, Resistor_SMD:R_0603_1608Metric_Pad0.98x0.95mm_HandSolder, F.Cu at (114.0, 90.2)
- added R362: 2K2, Resistor_SMD:R_0603_1608Metric_Pad0.98x0.95mm_HandSolder, F.Cu at (115.6, 90.2)
- added R363: 2K2, Resistor_SMD:R_0603_1608Metric_Pad0.98x0.95mm_HandSolder, F.Cu at (118.2, 89.4)
- added R364: 2K2, Resistor_SMD:R_0603_1608Metric_Pad0.98x0.95mm_HandSolder, F.Cu at (114.0, 86.8)
- added R365: 2K2, Resistor_SMD:R_0603_1608Metric_Pad0.98x0.95mm_HandSolder, F.Cu at (115.6, 86.8)
- added R366: 2K2, Resistor_SMD:R_0603_1608Metric_Pad0.98x0.95mm_HandSolder, F.Cu at (118.2, 86.0)
- added R367: 2K2, Resistor_SMD:R_0603_1608Metric_Pad0.98x0.95mm_HandSolder, F.Cu at (114.0, 83.4)
- added R368: 2K2, Resistor_SMD:R_0603_1608Metric_Pad0.98x0.95mm_HandSolder, F.Cu at (115.6, 83.4)
- added R369: 2K2, Resistor_SMD:R_0603_1608Metric_Pad0.98x0.95mm_HandSolder, F.Cu at (118.2, 82.6)
- added R370: 2K2, Resistor_SMD:R_0603_1608Metric_Pad0.98x0.95mm_HandSolder, F.Cu at (111.2, 76.8)
- added R371: 100, Resistor_SMD:R_0603_1608Metric_Pad0.98x0.95mm_HandSolder, F.Cu at (128.8, 70.4)
- added R372: 100, Resistor_SMD:R_0603_1608Metric_Pad0.98x0.95mm_HandSolder, F.Cu at (135.8, 70.4)
- added R515: 1K, Resistor_SMD:R_0603_1608Metric_Pad0.98x0.95mm_HandSolder, F.Cu at (180.4, 117.4)
- added R516: 10K, Resistor_SMD:R_0603_1608Metric_Pad0.98x0.95mm_HandSolder, F.Cu at (183.6, 135.4)
- added R517: 1K, Resistor_SMD:R_0603_1608Metric_Pad0.98x0.95mm_HandSolder, F.Cu at (180.4, 135.4)
- added R518: 10K, Resistor_SMD:R_0603_1608Metric_Pad0.98x0.95mm_HandSolder, F.Cu at (192.6, 126.4)
- added R519: 1K, Resistor_SMD:R_0603_1608Metric_Pad0.98x0.95mm_HandSolder, F.Cu at (189.4, 126.4)
- added R520: RUSB, Resistor_SMD:R_0603_1608Metric_Pad0.98x0.95mm_HandSolder, F.Cu at (155.2, 81.0)
- added R521: 1K, Resistor_SMD:R_0603_1608Metric_Pad0.98x0.95mm_HandSolder, F.Cu at (194.2, 69.2)
- added R522: 1K, Resistor_SMD:R_0603_1608Metric_Pad0.98x0.95mm_HandSolder, F.Cu at (189.0, 69.2)
- added R523: 1K, Resistor_SMD:R_0603_1608Metric_Pad0.98x0.95mm_HandSolder, F.Cu at (185.0, 69.2)
- added R524: 1K, Resistor_SMD:R_0603_1608Metric_Pad0.98x0.95mm_HandSolder, F.Cu at (185.0, 67.6)
- added R525: 10K, Resistor_SMD:R_0603_1608Metric_Pad0.98x0.95mm_HandSolder, F.Cu at (187.0, 92.0)
- added R526: 10K, Resistor_SMD:R_0603_1608Metric_Pad0.98x0.95mm_HandSolder, F.Cu at (187.0, 97.2)
- added R527: 10K, Resistor_SMD:R_0603_1608Metric_Pad0.98x0.95mm_HandSolder, F.Cu at (183.4, 92.0)
- added R528: 10K, Resistor_SMD:R_0603_1608Metric_Pad0.98x0.95mm_HandSolder, F.Cu at (183.4, 97.2)
- C101, C104, C105, C106, C301, C302: footprint Capacitor_SMD:C_0603_1608Metric_Pad1.05x0.95mm_HandSolder -> Capacitor_SMD:C_1206_3216Metric_Pad1.33x1.80mm_HandSolder
- C102, C201, C202, C203, C204, C205, C401, C402, C403, C404, C501, C502, C503, C504: footprint Capacitor_SMD:C_0603_1608Metric_Pad1.05x0.95mm_HandSolder -> Capacitor_SMD:C_0603_1608Metric_Pad1.08x0.95mm_HandSolder
- C303, C304: value 10n -> 4n7; footprint Capacitor_SMD:C_0603_1608Metric_Pad1.05x0.95mm_HandSolder -> Capacitor_SMD:C_0603_1608Metric_Pad1.08x0.95mm_HandSolder
- C305, C306, C307, C308: footprint Capacitor_SMD:C_0603_1608Metric_Pad1.05x0.95mm_HandSolder -> Capacitor_SMD:C_0805_2012Metric_Pad1.18x1.45mm_HandSolder
- D501: value RX -> WS2812B; footprint LED_SMD:LED_0603_1608Metric_Pad1.05x0.95mm_HandSolder -> LED_SMD:LED_WS2812B_PLCC4_5.0x5.0mm_P3.2mm; moved to B.Cu
- D502: value TX -> WS2812B; footprint LED_SMD:LED_0603_1608Metric_Pad1.05x0.95mm_HandSolder -> LED_SMD:LED_WS2812B_PLCC4_5.0x5.0mm_P3.2mm; moved to B.Cu
- D503: value LOAD -> WS2812B; footprint LED_SMD:LED_0603_1608Metric_Pad1.05x0.95mm_HandSolder -> LED_SMD:LED_WS2812B_PLCC4_5.0x5.0mm_P3.2mm; moved to B.Cu
- DS501: footprint KSK_HeikouBox:OLED-4P-Generic-128x32-0.91in -> KSK_HeikouBox:OLED-4P-Generic-128x64-0.96in
- F101: value Poly 0.5A -> Poly 1A
- J101: value Barrel_Jack_Switch -> 5V
- J302: footprint KSK_HeikouBox:Jack_3.5mm_PJ307_Horizontal_NoHoles -> KSK_HeikouBox:Jack_3.5mm_PJ307_Horizontal
- J501: value USB_B_Micro -> Micro_SD_Card_TFP09-2-12B; footprint KSK_HeikouBox:USB_Mini-Micro-B_Multi -> KSK_HeikouBox:Micro_SD_Card_TFP09-2-12B
- J502: value Micro_SD_Card_Det -> RGB; footprint Connector_Card:microSD_HC_Hirose_DM3D-SF -> Connector_PinHeader_2.54mm:PinHeader_1x03_P2.54mm_Vertical
- JP101: value SolderJumper_3_Bridged12 -> Power; footprint Jumper:SolderJumper-3_P1.3mm_Bridged12_Pad1.0x1.5mm -> Connector_PinHeader_2.54mm:PinHeader_1x03_P2.54mm_Vertical
- Q501: value MMBT3906 -> BSS138
- R101, R201, R202, R203, R204, R205, R206, R207, R208, R209, R210, R301, R302, R303, R304, R305, R306, R307, R308, R309, R310, R311, R312, R319, R320, R401, R402, R403, R404, R405, R501, R502, R503, R504, R505, R506, R507, R508, R512, R514: footprint Resistor_SMD:R_0603_1608Metric_Pad1.05x0.95mm_HandSolder -> Resistor_SMD:R_0603_1608Metric_Pad0.98x0.95mm_HandSolder
- R313, R314, R510: value 1K -> 2K2; footprint Resistor_SMD:R_0603_1608Metric_Pad1.05x0.95mm_HandSolder -> Resistor_SMD:R_0603_1608Metric_Pad0.98x0.95mm_HandSolder
- R315, R316, R509: value 1K -> 10K; footprint Resistor_SMD:R_0603_1608Metric_Pad1.05x0.95mm_HandSolder -> Resistor_SMD:R_0603_1608Metric_Pad0.98x0.95mm_HandSolder
- R317, R318: value 10K -> 4K7; footprint Resistor_SMD:R_0603_1608Metric_Pad1.05x0.95mm_HandSolder -> Resistor_SMD:R_0603_1608Metric_Pad0.98x0.95mm_HandSolder
- R321, R322, R513: value 10K -> 1K; footprint Resistor_SMD:R_0603_1608Metric_Pad1.05x0.95mm_HandSolder -> Resistor_SMD:R_0603_1608Metric_Pad0.98x0.95mm_HandSolder
- R511: value 10K -> 2K2; footprint Resistor_SMD:R_0603_1608Metric_Pad1.05x0.95mm_HandSolder -> Resistor_SMD:R_0603_1608Metric_Pad0.98x0.95mm_HandSolder
- SW501: value SW_Push -> Left
- SW502: value SW_Push -> Up
- SW503: value SW_Push -> Down
- SW504: value SW_Push -> Right
- U501: value ATmega644PA-AU -> STM32-BluePill-Socket; footprint Package_QFP:TQFP-44_10x10mm_P0.8mm -> KSK_HeikouBox:STM32-BluePill-Socket
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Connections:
- C301 pad 1: /part1-power/5V -> /part1-power/3V3
- C302 pad 1: /part1-power/5V -> /part1-power/3V3
- C501 pad 2: /part1-power/GND -> Net-(C501-Pad2)
- C502 pad 2: /part1-power/GND -> Net-(C502-Pad2)
- C503 pad 2: /part1-power/GND -> Net-(C503-Pad2)
- C504 pad 2: /part1-power/GND -> Net-(C504-Pad2)
- D501 pad 1: Net-(D501-Pad1) -> /part1-power/5V
- D502 pad 1: Net-(D502-Pad1) -> /part1-power/5V
- D503 pad 1: Net-(D503-Pad1) -> /part1-power/5V
- DS501 pad 1: /part1-power/GND -> Net-(DS501-Pad1)
- DS501 pad 2: /part1-power/3V3 -> Net-(DS501-Pad2)
- F101 pad 1: /part1-power/VUSB -> /part1-power/5V
- J101 pad 3: /part1-power/GND -> Net-(J101-Pad3)
- J302 pad R: Net-(C308-Pad1) -> Net-(J302-PadR)
- J302 pad RN: Net-(C308-Pad1) -> Net-(J302-PadR)
- J302 pad T: Net-(C307-Pad1) -> Net-(J302-PadT)
- J302 pad TN: Net-(C307-Pad1) -> Net-(J302-PadT)
- J501 pad 1: /part1-power/VUSB -> Net-(J501-Pad1)
- J501 pad 4: Net-(J501-Pad4) -> /part1-power/3V3
- J501 pad 5: /part1-power/GND -> Net-(J501-Pad5)
- J502 pad 1: Net-(J502-Pad1) -> /part1-power/5V
- J502 pad 3: Net-(J502-Pad3) -> /part1-power/GND
- JP101 pad 2: /part1-power/5V -> Net-(F101-Pad2)
- JP101 pad 3: Net-(F101-Pad2) -> /part1-power/VUSB
- Q301 pad 3: /part1-power/5V -> /part1-power/3V3
- Q302 pad 3: /part1-power/5V -> /part1-power/3V3
- Q303 pad 3: /part1-power/5V -> /part1-power/3V3
- Q304 pad 3: Net-(J301-Pad14) -> Net-(J301-Pad13)
- Q305 pad 3: Net-(J301-Pad13) -> Net-(J301-Pad14)
- Q306 pad 3: /part1-power/5V -> /part1-power/3V3
- Q307 pad 3: /part1-power/5V -> /part1-power/3V3
- Q501 pad 1: Net-(Q501-Pad1) -> /part1-power/3V3
- R304 pad 1: Net-(R304-Pad1) -> Net-(Q301-Pad1)
- R304 pad 2: Net-(Q301-Pad2) -> Net-(R304-Pad2)
- R305 pad 1: Net-(R305-Pad1) -> Net-(Q302-Pad1)
- R305 pad 2: Net-(Q302-Pad2) -> Net-(R305-Pad2)
- R306 pad 1: Net-(R306-Pad1) -> Net-(Q303-Pad1)
- R306 pad 2: Net-(Q303-Pad2) -> Net-(R306-Pad2)
- R307 pad 2: /part3-av/NVSYNC -> /part3-av/NHSYNC
- R308 pad 2: /part3-av/NHSYNC -> /part3-av/NVSYNC
- R309 pad 1: Net-(Q304-Pad1) -> /part1-power/GND
- R309 pad 2: /part1-power/GND -> Net-(Q304-Pad1)
- R310 pad 1: Net-(Q305-Pad1) -> /part1-power/GND
- R310 pad 2: /part1-power/GND -> Net-(Q305-Pad1)
- R311 pad 1: /part1-power/5V -> Net-(J301-Pad13)
- R311 pad 2: Net-(J301-Pad14) -> /part1-power/5V
- R312 pad 1: /part1-power/5V -> Net-(J301-Pad14)
- R312 pad 2: Net-(J301-Pad13) -> /part1-power/5V
- R315 pad 1: Net-(C307-Pad2) -> Net-(C305-Pad2)
- R315 pad 2: /part1-power/GND -> Net-(C303-Pad1)
- R316 pad 1: Net-(C308-Pad2) -> Net-(C306-Pad2)
- R316 pad 2: /part1-power/GND -> Net-(C304-Pad1)
- R317 pad 1: Net-(C305-Pad2) -> /part1-power/3V3
- R317 pad 2: Net-(C303-Pad1) -> Net-(C305-Pad1)
- R318 pad 1: Net-(C306-Pad2) -> /part1-power/3V3
- R318 pad 2: Net-(C304-Pad1) -> Net-(C306-Pad1)
- R319 pad 1: /part1-power/5V -> Net-(C305-Pad1)
- R319 pad 2: Net-(C305-Pad1) -> /part1-power/GND
- R320 pad 1: /part1-power/5V -> Net-(C306-Pad1)
- R320 pad 2: Net-(C306-Pad1) -> /part1-power/GND
- R321 pad 1: Net-(C305-Pad1) -> Net-(C307-Pad2)
- R322 pad 1: Net-(C306-Pad1) -> Net-(C308-Pad2)
- R501 pad 1: /part1-power/3V3 -> Net-(R501-Pad1)
- R501 pad 2: Net-(D501-Pad2) -> /part2-core/mdb0
- R502 pad 1: /part1-power/3V3 -> Net-(R502-Pad1)
- R502 pad 2: Net-(D502-Pad2) -> /part2-core/mdb1
- R503 pad 1: /part1-power/3V3 -> Net-(R503-Pad1)
- R503 pad 2: Net-(D503-Pad2) -> /part2-core/mdb2
- R504 pad 1: /part1-power/3V3 -> Net-(R504-Pad1)
- R504 pad 2: Net-(J502-Pad2) -> /part2-core/mdb3
- R505 pad 2: Net-(C509-Pad1) -> /part2-core/mdb4
- R506 pad 2: Net-(C510-Pad1) -> /part2-core/mdb5
- R507 pad 2: Net-(C511-Pad1) -> /part2-core/mdb6
- R508 pad 2: Net-(C512-Pad1) -> /part2-core/mdb7
- R509 pad 1: Net-(Q501-Pad3) -> Net-(J501-Pad2)
- R509 pad 2: Net-(R509-Pad2) -> /part1-power/3V3
- R510 pad 1: /part2-core/mdb4 -> Net-(DS501-Pad3)
- R510 pad 2: Net-(Q501-Pad3) -> /part1-power/3V3
- R511 pad 1: Net-(C509-Pad1) -> Net-(DS501-Pad4)
- R512 pad 1: Net-(C510-Pad1) -> /part1-power/3V3
- R512 pad 2: /part1-power/3V3 -> Net-(C501-Pad2)
- R513 pad 1: Net-(C511-Pad1) -> Net-(R513-Pad1)
- R513 pad 2: /part1-power/3V3 -> Net-(C501-Pad2)
- R514 pad 1: Net-(C512-Pad1) -> /part1-power/3V3
- R514 pad 2: /part1-power/3V3 -> Net-(C502-Pad2)
- RV301 pad 1: Net-(R304-Pad1) -> /part1-power/GND
- RV301 pad 2: /part1-power/GND -> Net-(R304-Pad2)
- RV301 pad 3: /part1-power/GND -> Net-(R304-Pad2)
- RV302 pad 1: Net-(R305-Pad1) -> /part1-power/GND
- RV302 pad 2: /part1-power/GND -> Net-(R305-Pad2)
- RV302 pad 3: /part1-power/GND -> Net-(R305-Pad2)
- RV303 pad 1: Net-(R306-Pad1) -> /part1-power/GND
- RV303 pad 2: /part1-power/GND -> Net-(R306-Pad2)
- RV303 pad 3: /part1-power/GND -> Net-(R306-Pad2)
- SW501 pad 1: Net-(R505-Pad1) -> Net-(R513-Pad1)
- SW502 pad 1: Net-(R506-Pad1) -> Net-(R515-Pad1)
- SW503 pad 1: Net-(R507-Pad1) -> Net-(R517-Pad1)
- SW504 pad 1: Net-(R508-Pad1) -> Net-(R519-Pad1)
- U103 pad 3: /part1-power/3V3 -> /part1-power/5V
- U202 pad 10: Net-(U202-Pad10) -> /part2-core/clk_28
- U202 pad 11: /part1-power/GND -> Net-(R202-Pad1)
- U202 pad 12: Net-(U202-Pad12) -> Net-(R202-Pad1)
- U202 pad 13: /part1-power/GND -> Net-(C204-Pad1)
- U202 pad 5: Net-(C204-Pad1) -> /part1-power/GND
- U202 pad 6: Net-(R202-Pad1) -> Net-(U202-Pad6)
- U202 pad 8: /part2-core/clk_28 -> Net-(U202-Pad8)
- U202 pad 9: Net-(R202-Pad1) -> /part1-power/GND
- U501 pad 1: Net-(J502-Pad3) -> Net-(U501-Pad1)
- U501 pad 10: Net-(U501-Pad10) -> Net-(J501-Pad5)
- U501 pad 11: Net-(RN501-Pad2) -> Net-(J501-Pad7)
- U501 pad 12: Net-(Q501-Pad2) -> Net-(J501-Pad3)
- U501 pad 13: /part2-core/cfg_DCLK -> /part4-memory/XCLK
- U501 pad 14: Net-(C512-Pad1) -> /part4-memory/XWE
- U501 pad 15: Net-(C511-Pad1) -> Net-(R508-Pad1)
- U501 pad 16: Net-(C510-Pad1) -> Net-(R507-Pad1)
- U501 pad 17: /part1-power/3V3 -> Net-(U501-Pad17)
- U501 pad 18: /part1-power/GND -> Net-(U501-Pad18)
- U501 pad 19: Net-(DS501-Pad3) -> /part1-power/GND
- U501 pad 2: Net-(J502-Pad7) -> Net-(Q502-Pad2)
- U501 pad 20: Net-(DS501-Pad4) -> /part1-power/GND
- U501 pad 21: Net-(RN501-Pad3) -> Net-(R506-Pad1)
- U501 pad 22: Net-(RN501-Pad4) -> /part2-core/cfg_DCLK
- U501 pad 23: Net-(R509-Pad2) -> Net-(R504-Pad1)
- U501 pad 24: Net-(RN502-Pad1) -> Net-(R505-Pad1)
- U501 pad 25: Net-(RN502-Pad2) -> Net-(R503-Pad1)
- U501 pad 26: Net-(RN502-Pad3) -> Net-(R501-Pad1)
- U501 pad 27: /part1-power/3V3 -> Net-(R502-Pad1)
- U501 pad 28: /part1-power/GND -> Net-(U501-Pad28)
- U501 pad 3: Net-(J502-Pad5) -> Net-(J501-Pad9)
- U501 pad 30: /part5-hub/kb_C -> /part4-memory/CKE
- U501 pad 31: /part5-hub/kb_D -> /part4-memory/XCAS
- U501 pad 32: /part5-hub/gp_D2 -> /part2-core/cfg_DONE
- U501 pad 33: /part5-hub/gp_D1 -> /part2-core/cfg_NSTAT
- U501 pad 34: /part4-memory/XWE -> Net-(DS501-Pad3)
- U501 pad 35: /part4-memory/XCAS -> Net-(DS501-Pad4)
- U501 pad 36: /part4-memory/XCLK -> Net-(Q503-Pad2)
- U501 pad 37: /part4-memory/CKE -> /part2-core/cfg_NCFG
- U501 pad 38: /part1-power/3V3 -> /part1-power/VUSB
- U501 pad 4: Net-(C509-Pad1) -> Net-(C501-Pad2)
- U501 pad 40: Net-(D503-Pad1) -> Net-(U501-Pad40)
- U501 pad 5: /part1-power/3V3 -> Net-(Q501-Pad2)
- U501 pad 6: /part1-power/GND -> Net-(C502-Pad2)
- U501 pad 7: Net-(C508-Pad1) -> Net-(C503-Pad2)
- U501 pad 8: Net-(C507-Pad1) -> Net-(C504-Pad2)
- U501 pad 9: Net-(U501-Pad9) -> Net-(J501-Pad2)
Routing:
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- added copper zone on B.Cu, net /part1-power/GND
- added copper zone on F.Cu, net /part1-power/GND
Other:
- board outline added: 100 x 100 mm
- board text added: "1 2"
- board text added: "5 RGB 0"
- board text added: "5V 1A"
- board text added: "EXTRA BUS"
- board text added: "JTAG"
- board text added: "KEYBOARD"
- board text added: "LINE OUT"
- board text added: "MICRO SD"
- board text added: "R G B"
- board text added: "USB"
- board text added: "VCC GND"
- board text added: "VGA"
